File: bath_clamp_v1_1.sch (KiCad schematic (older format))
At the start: 70 parts, among them J1 105-1103-001, J2 105-1103-001, J3 105-1103-001, K1 1462042-8, K2 1462042-8, Q1 MBT3904DW1T1G, Q3 MBT3904DW1T1G, Q4 MBT3904DW1T1G, U1 OPA828, U12 TCA9555DBR, U13 TCA9555DBR, U2 ADG1208, U3 G6L-1F-TR-DC5, U4 G6L-1F-TR-DC5, U5 G6L-1F-TR-DC5

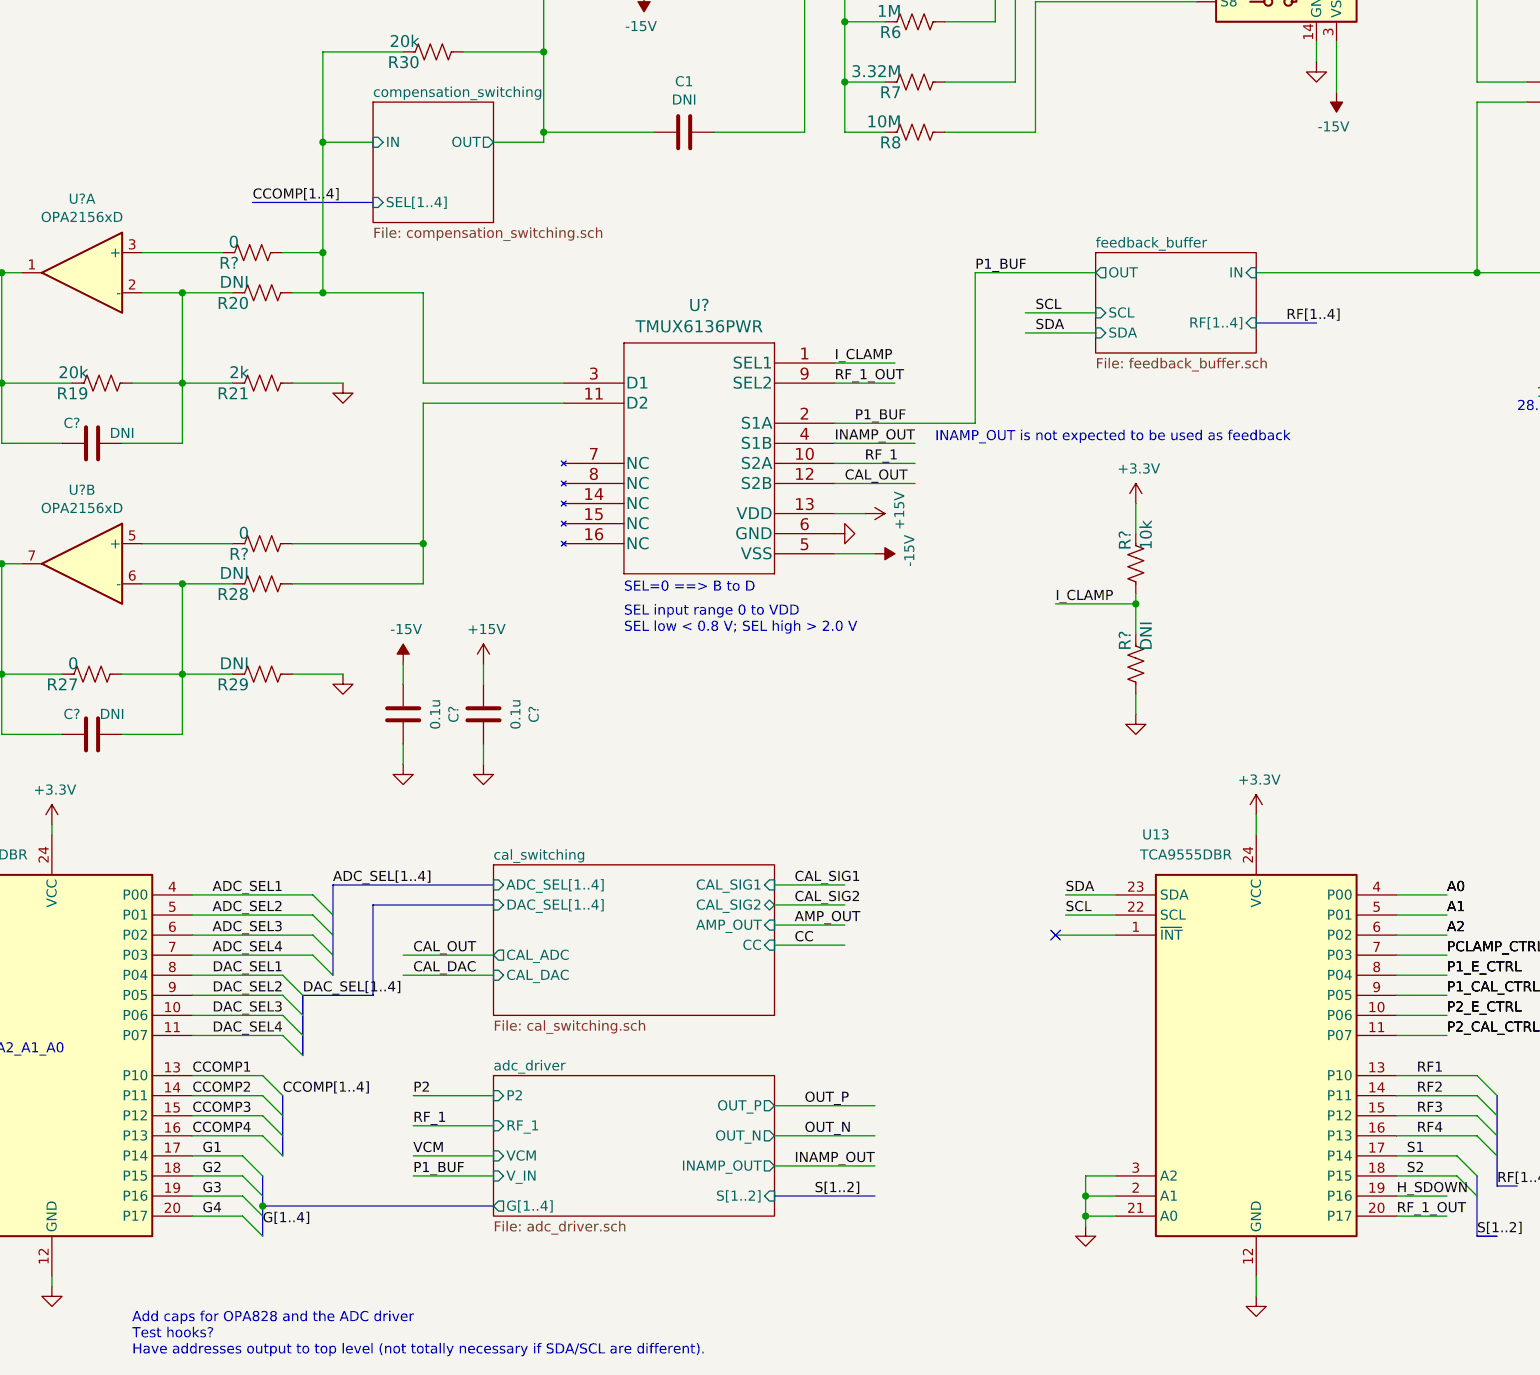
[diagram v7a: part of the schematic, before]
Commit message: added pdf print of schematics
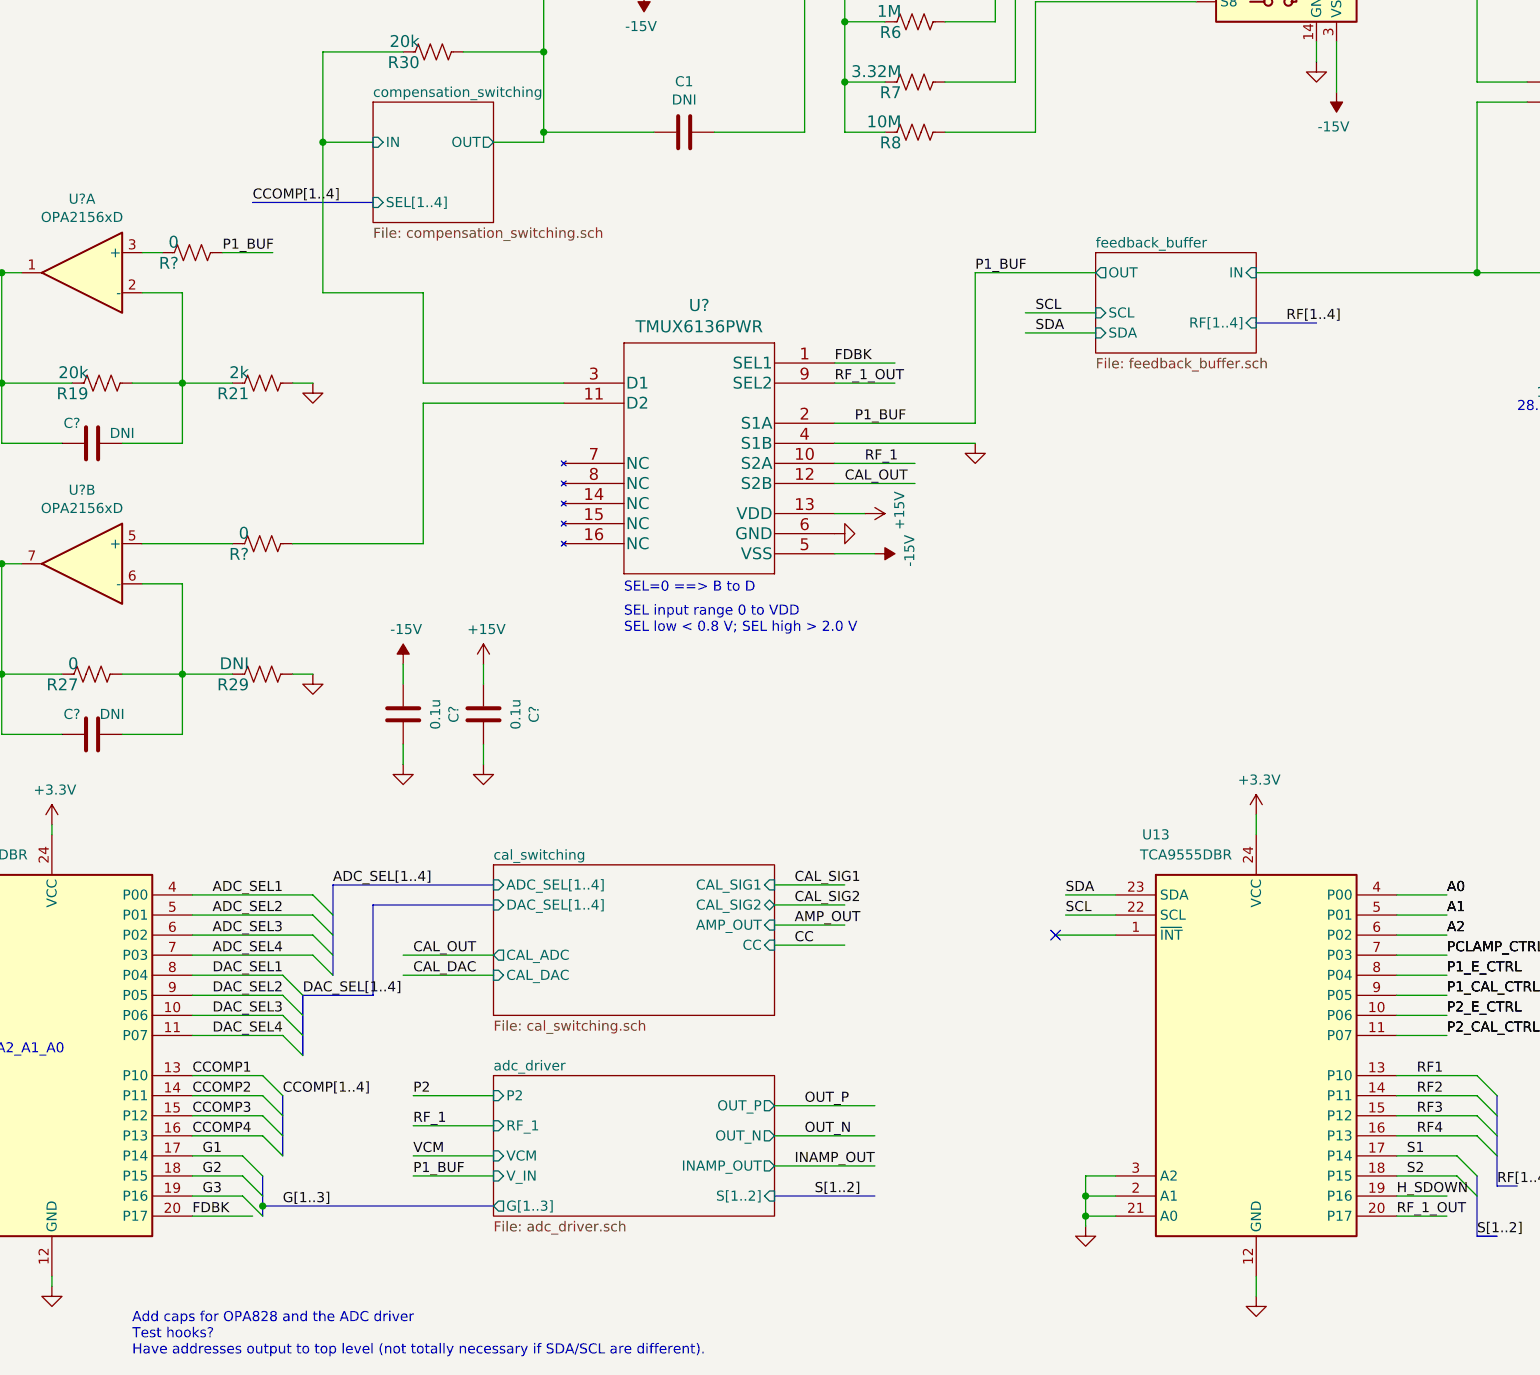
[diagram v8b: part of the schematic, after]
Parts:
- removed R20, R28, R?: DNI, Resistor_SMD:R_0603_1608Metric, symbol Device:R_US
- removed R?: 10k, Resistor_SMD:R_0603_1608Metric, symbol Device:R_US
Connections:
- net labels added: FDBK, G[1..3]
- net labels removed: G4, G[1..4], I_CLAMP
- wire segments 358 -> 347
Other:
- note removed: "INAMP_OUT is not expected to be used as feedback\n"
- moved on the sheet: R?
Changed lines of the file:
@@
-$EndComp
-$Comp
-L Device:R_US R20
-U 1 1 60742525
-P 3150 5050
-F 0 "R20" V 3097 5118 59  0000 L CNN
-F 1 "DNI" V 3202 5118 59  0000 L CNN
-F 2 "Resistor_SMD:R_0603_1608Metric" H 3150 5050 50  0001 C CNN
-F 3 "" H 3150 5050 50  0001 C CNN
-F 4 "" H 3097 5218 50  0001 C CNN "Manf#"
-F 5 "1%" H 3150 5050 50  0001 C CNN "Tolerance"
-	1    3150 5050
-	0    -1   -1   0
 $EndComp
 $Comp
@@
 	1    2100 10000
 	1    0    0    -1
-$EndComp
-$Comp
-L Device:R_US R28
-U 1 1 60AFE691
-P 3150 6500
-F 0 "R28" V 3097 6568 59  0000 L CNN
-F 1 "DNI" V 3202 6568 59  0000 L CNN
-F 2 "Resistor_SMD:R_0603_1608Metric" H 3150 6500 50  0001 C CNN
-F 3 "" H 3150 6500 50  0001 C CNN
-F 4 "RC0603FR-0773K2L" H 3097 6668 50  0001 C CNN "Manf#"
-F 5 "1%" H 3150 6500 50  0001 C CNN "Tolerance"
-	1    3150 6500
-	0    -1   -1   0
 $EndComp
 $Comp
@@
 Text Label 2850 9550 0    50   ~ 0
 G3
-Text Label 2850 9650 0    50   ~ 0
-G4
-Text Label 3150 9700 0    50   ~ 0
-G[1..4]
+Text Label 2800 9650 0    50   ~ 0
+FDBK
+Text Label 3250 9600 0    50   ~ 0
+G[1..3]
 Text Label 3900 9050 0    50   ~ 0
 P2
@@
 	3450 3850 3450 4300
 Wire Wire Line
-	3450 4300 3700 4300
-Wire Wire Line
 	3450 3850 3850 3850
 Wire Wire Line
 	2750 5500 3000 5500
 Wire Wire Line
-	2750 5050 3000 5050
-Wire Wire Line
 	2750 5050 2550 5050
 Wire Wire Line
@@
 	850  4950 1500 4950
 Wire Wire Line
-	3300 5500 3550 5500
-Wire Wire Line
-	3300 5050 3450 5050
+	3300 5500 3400 5500
 Wire Wire Line
 	8800 8050 9050 8050
@@
 	2750 6950 3000 6950
 Wire Wire Line
-	2750 6500 3000 6500
-Wire Wire Line
 	2750 6500 2550 6500
 Wire Wire Line
@@
 	850  6400 1500 6400
 Wire Wire Line
-	3300 6950 3550 6950
+	3300 6950 3400 6950
 Wire Wire Line
 	2150 6950 1850 6950
@@
 Entry Wire Line
 	3050 9550 3150 9650
-Entry Wire Line
-	3050 9650 3150 9750
 Entry Wire Line
 	3400 8050 3500 8150
@@
 Connection ~ 5850 3200
 Connection ~ 4550 4250
-Connection ~ 3450 4300
 Connection ~ 2750 5500
-Connection ~ 2750 5050
 Connection ~ 4550 3850
 Connection ~ 7250 9550
@@
 Connection ~ 1850 4950
 Connection ~ 2750 6950
-Connection ~ 2750 6500
 Connection ~ 1850 6400
 Connection ~ 3150 9600
@@
 Wire Wire Line
 	1150 8150 1400 8150
-Wire Wire Line
-	2800 9650 3050 9650
 Wire Wire Line
 	2800 9550 3050 9550
@@
 F1 "adc_driver.sch" 50
 F2 "P2" I L 4300 9050 50
-F3 "G[1..4]" O L 4300 9600 50
-F4 "VCM" I L 4300 9350 50
-F5 "OUT_N" O R 5700 9250 50
-F6 "INAMP_OUT" O R 5700 9400 50
-F7 "V_IN" I L 4300 9450 50
-F8 "S[1..2]" I R 5700 9550 50
-F9 "OUT_P" O R 5700 9100 50
-F10 "RF_1" I L 4300 9200 50
+F3 "VCM" I L 4300 9350 50
+F4 "OUT_N" O R 5700 9250 50
+F5 "INAMP_OUT" O R 5700 9400 50
+F6 "V_IN" I L 4300 9450 50
+F7 "S[1..2]" I R 5700 9550 50
+F8 "OUT_P" O R 5700 9100 50
+F9 "RF_1" I L 4300 9200 50
+F10 "G[1..3]" O L 4300 9600 50
 $EndSheet
 Wire Wire Line
@@
 INAMP_OUT
 Wire Wire Line
-	6000 5800 6400 5800
-Text Label 6000 5800 0    50   ~ 0
-INAMP_OUT
-Wire Wire Line
 	6000 5700 6700 5700
 Text Label 6100 5700 0    50   ~ 0
 P1_BUF
 Wire Wire Line
-	4650 5500 3950 5500
-Wire Wire Line
-	3450 4300 3450 4850
-Wire Wire Line
 	7300 4950 6700 4950
 Wire Wire Line
 	6700 4950 6700 5700
-Wire Wire Line
-	3950 5050 3450 5050
-Wire Wire Line
-	3950 5050 3950 5500
-Connection ~ 3450 5050
 Wire Wire Line
 	8800 9550 9050 9550
@@
 	6000 5400 6300 5400
 Text Label 6000 5400 0    50   ~ 0
-I_CLAMP
+FDBK
 Wire Wire Line
 	6000 5900 6400 5900
@@
 Wire Wire Line
 	4650 5600 3950 5600
-Wire Wire Line
-	3300 6500 3950 6500
 Wire Wire Line
 	6000 5500 6300 5500
@@
 L power:GND #PWR?
 U 1 1 610AF0A4
-P 3550 6950
-F 0 "#PWR?" H 3550 6700 50  0001 C CNN
-F 1 "GND" V 3555 6822 50  0001 R CNN
-F 2 "" H 3550 6950 50  0001 C CNN
-F 3 "" H 3550 6950 50  0001 C CNN
-	1    3550 6950
+P 3400 6950
+F 0 "#PWR?" H 3400 6700 50  0001 C CNN
+F 1 "GND" V 3405 6822 50  0001 R CNN
+F 2 "" H 3400 6950 50  0001 C CNN
+F 3 "" H 3400 6950 50  0001 C CNN
+	1    3400 6950
 	1    0    0    -1
 $EndComp
@@
 L power:GND #PWR?
 U 1 1 610AF625
-P 3550 5500
-F 0 "#PWR?" H 3550 5250 50  0001 C CNN
-F 1 "GND" V 3555 5372 50  0001 R CNN
-F 2 "" H 3550 5500 50  0001 C CNN
-F 3 "" H 3550 5500 50  0001 C CNN
-	1    3550 5500
+P 3400 5500
+F 0 "#PWR?" H 3400 5250 50  0001 C CNN
+F 1 "GND" V 3405 5372 50  0001 R CNN
+F 2 "" H 3400 5500 50  0001 C CNN
+F 3 "" H 3400 5500 50  0001 C CNN
+	1    3400 5500
 	1    0    0    -1
 $EndComp
@@
 Wire Wire Line
 	3300 6300 3950 6300
-Connection ~ 3950 6300
-Wire Wire Line
-	3950 6300 3950 6500
 $Comp
 L Device:R_US R?
 U 1 1 6114E2FC
-P 3100 4850
-F 0 "R?" V 3047 4918 59  0000 L CNN
-F 1 "0" V 3152 4918 59  0000 L CNN
-F 2 "Resistor_SMD:R_0603_1608Metric" H 3100 4850 50  0001 C CNN
-F 3 "" H 3100 4850 50  0001 C CNN
-F 4 "RC0603FR-070RL" H 3047 5018 50  0001 C CNN "Manf#"
-F 5 "5%" H 3100 4850 50  0001 C CNN "Tolerance"
-	1    3100 4850
+P 2800 4850
+F 0 "R?" V 2747 4918 59  0000 L CNN
+F 1 "0" V 2852 4918 59  0000 L CNN
+F 2 "Resistor_SMD:R_0603_1608Metric" H 2800 4850 50  0001 C CNN
+F 3 "" H 2800 4850 50  0001 C CNN
+F 4 "RC0603FR-070RL" H 2747 5018 50  0001 C CNN "Manf#"
+F 5 "5%" H 2800 4850 50  0001 C CNN "Tolerance"
+	1    2800 4850
 	0    -1   -1   0
 $EndComp
 Wire Wire Line
-	2550 4850 2950 4850
-Wire Wire Line
-	3250 4850 3450 4850
-Connection ~ 3450 4850
-Wire Wire Line
-	3450 4850 3450 5050
+	2550 4850 2650 4850
 $Comp
 L Device:C C?
@@
 Text Notes 2150 3050 0    50   ~ 0
 Add a VIA or test hook
-Text Notes 6500 5800 0    50   ~ 0
-INAMP_OUT is not expected to be used as feedback\n
 Text Notes 4950 6550 0    50   ~ 0
 SEL=0 ==> B to D
@@
 Wire Wire Line
 	6400 1250 6400 1150
-$Comp
-L Device:R_US R?
-U 1 1 61F48A3B
-P 7500 6400
-F 0 "R?" V 7447 6468 59  0000 L CNN
-F 1 "10k" V 7552 6468 59  0000 L CNN
-F 2 "Resistor_SMD:R_0603_1608Metric" H 7500 6400 50  0001 C CNN
-F 3 "" H 7500 6400 50  0001 C CNN
-F 4 "RC0603FR-0710KL" H 7447 6568 50  0001 C CNN "Manf#"
-F 5 "5%" H 7500 6400 50  0001 C CNN "Tolerance"
-	1    7500 6400
-	1    0    0    -1
-$EndComp
-$Comp
-L Device:R_US R?
-U 1 1 61F9E802
-P 7500 6900
-F 0 "R?" V 7447 6968 59  0000 L CNN
-F 1 "DNI" V 7552 6968 59  0000 L CNN
-F 2 "Resistor_SMD:R_0603_1608Metric" H 7500 6900 50  0001 C CNN
-F 3 "" H 7500 6900 50  0001 C CNN
-F 4 "" H 7447 7068 50  0001 C CNN "Manf#"
-F 5 "5%" H 7500 6900 50  0001 C CNN "Tolerance"
-	1    7500 6900
-	1    0    0    -1
-$EndComp
-Wire Wire Line
-	7500 6550 7500 6600
-Wire Wire Line
-	7500 6750 7500 6600
-Connection ~ 7500 6600
-$Comp
-L power:+3.3V #PWR?
-U 1 1 62022426
-P 7500 6100
-F 0 "#PWR?" H 7500 5950 50  0001 C CNN
-F 1 "+3.3V" H 7515 6273 50  0000 C CNN
-F 2 "" H 7500 6100 50  0001 C CNN
-F 3 "" H 7500 6100 50  0001 C CNN
-	1    7500 6100
-	1    0    0    -1
-$EndComp
-Wire Wire Line
-	7500 6100 7500 6250
+Wire Bus Line
+	3150 9600 3150 9650
+Wire Wire Line
+	2800 9650 3100 9650
+Wire Wire Line
+	6000 5800 6700 5800
 $Comp
 L power:GND #PWR?
-U 1 1 6212692F
-P 7500 7150
-F 0 "#PWR?" H 7500 6900 50  0001 C CNN
-F 1 "GND" V 7505 7022 50  0001 R CNN
-F 2 "" H 7500 7150 50  0001 C CNN
-F 3 "" H 7500 7150 50  0001 C CNN
-	1    7500 7150
+U 1 1 624F19AC
+P 6700 5800
+F 0 "#PWR?" H 6700 5550 50  0001 C CNN
+F 1 "GND" V 6705 5672 50  0001 R CNN
+F 2 "" H 6700 5800 50  0001 C CNN
+F 3 "" H 6700 5800 50  0001 C CNN
+	1    6700 5800
 	-1   0    0    -1
 $EndComp
 Wire Wire Line
-	7500 7050 7500 7150
-Wire Wire Line
-	7100 6600 7500 6600
-Text Label 7100 6600 0    50   ~ 0
-I_CLAMP
+	2950 4850 3200 4850
+Text Label 2950 4850 0    50   ~ 0
+P1_BUF
+Wire Wire Line
+	4650 5500 3950 5500
+Wire Wire Line
+	3950 5500 3950 5050
+Wire Wire Line
+	3950 5050 3450 5050
+Wire Wire Line
+	3450 5050 3450 4300
+Connection ~ 3450 4300
+Wire Wire Line
+	3450 4300 3700 4300
 Wire Bus Line
 	9200 9450 9200 9750
 Wire Bus Line
-	3150 9600 3150 9750
-Wire Bus Line
 	3150 9450 3150 9600
